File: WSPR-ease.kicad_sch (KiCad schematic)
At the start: 31 parts, among them J1 GNSS Ant, J2 Tx Ant, J3 USB_C_16P_Stacked, Q1 MMBF170, U1 ESP32-S3-WROOM-1-N8R8, U2 NCP1117-3.3_SOT223, U3 ATGM336H-5N31

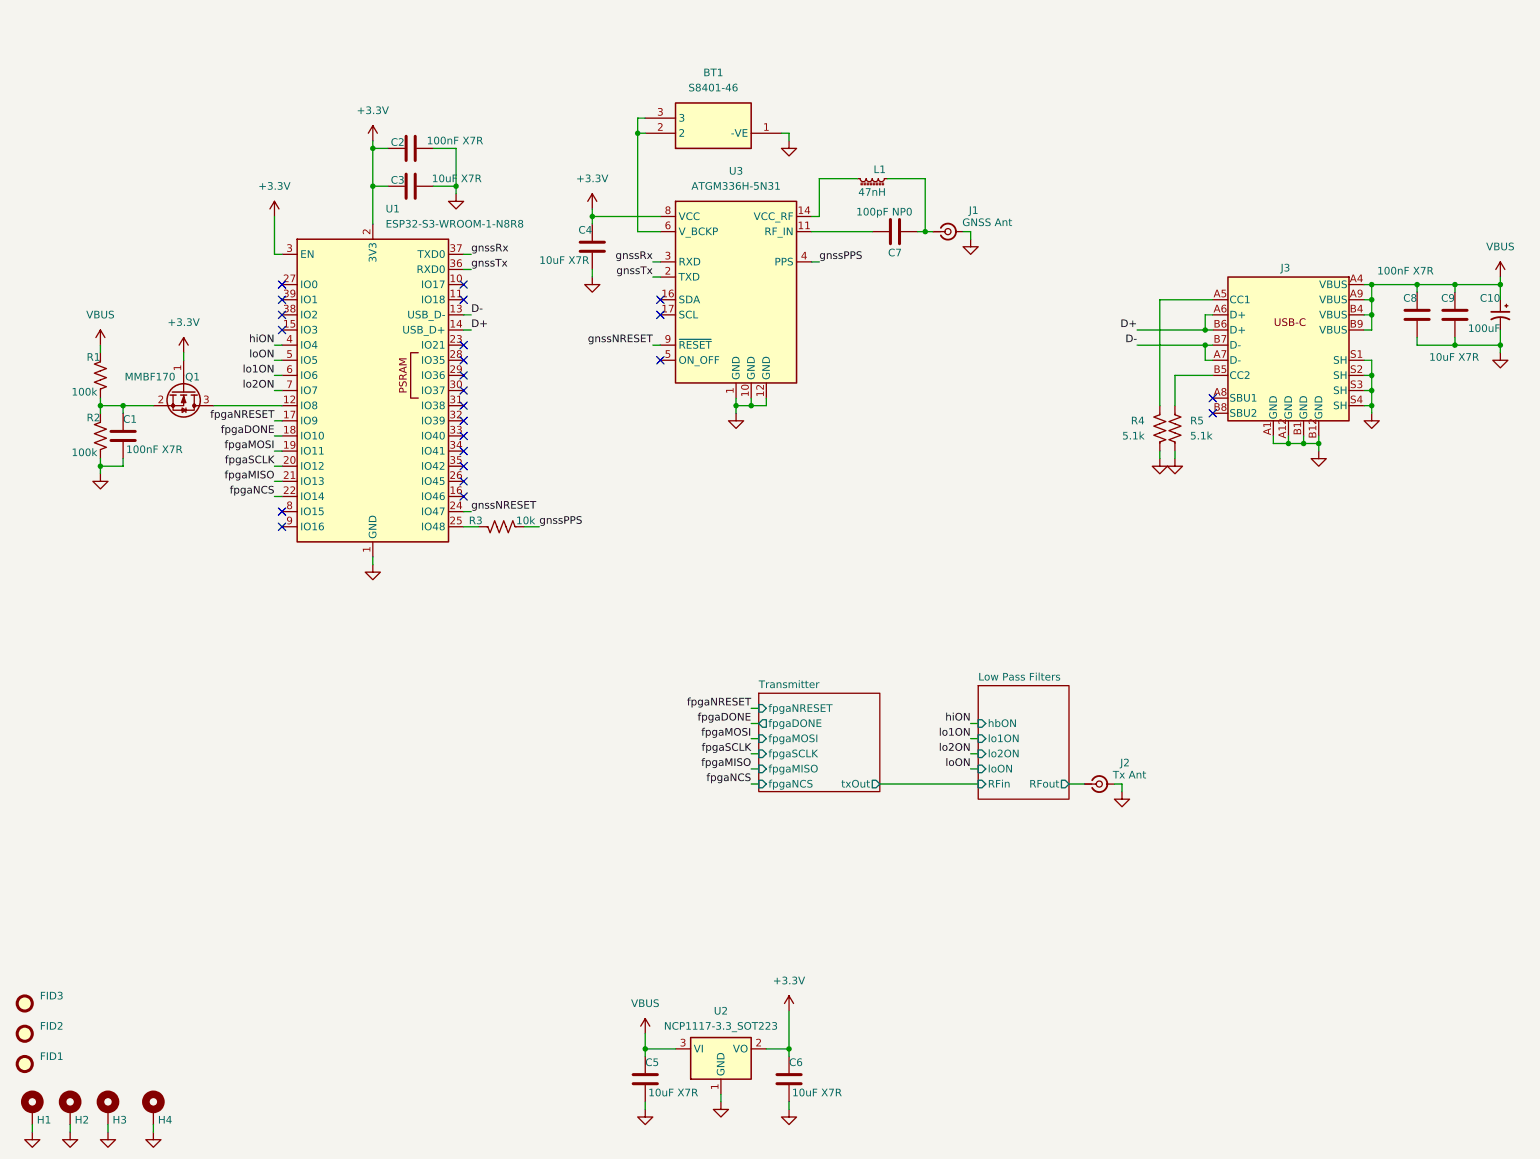
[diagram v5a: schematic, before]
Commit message: Cleanup. Better USB diff pair with 0ohm and TVS as recommended. Return to rectangular outline and even smaller. Mounting holes are consistently placed relative to board corners.
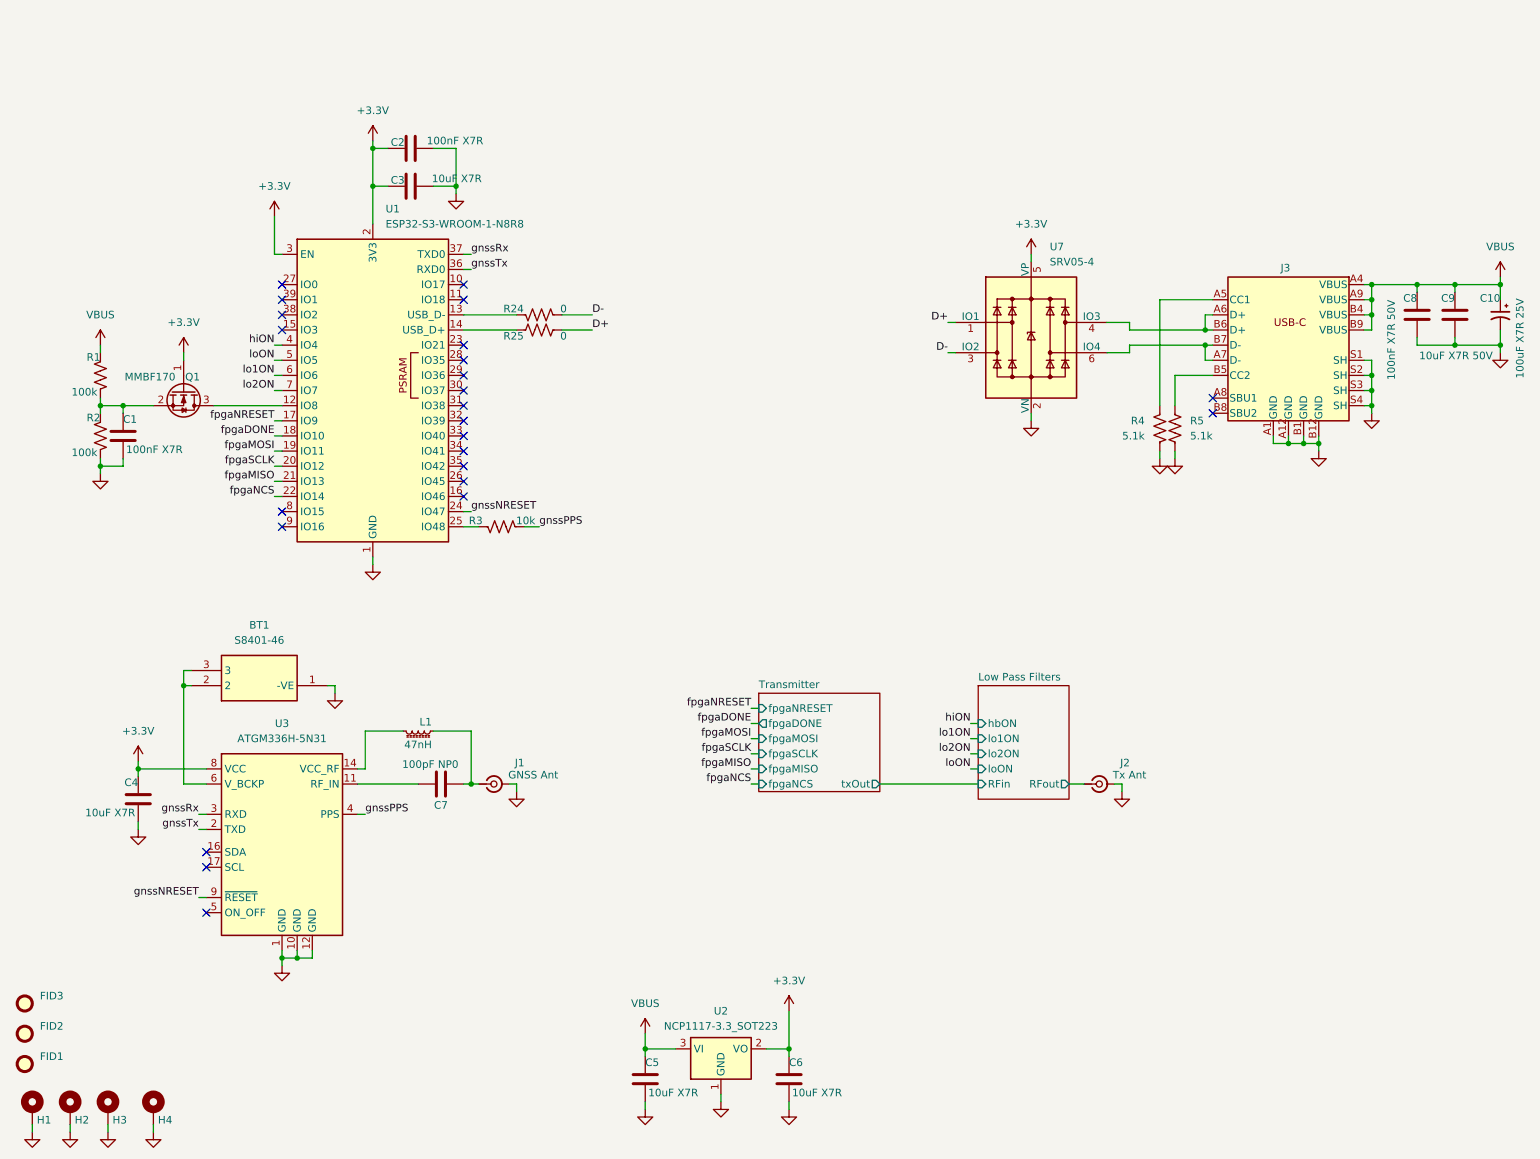
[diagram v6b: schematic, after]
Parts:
- added R24, R25: 0, Resistor_SMD:R_0402_1005Metric, symbol Device:R_US
- added U7: SRV05-4, Package_TO_SOT_SMD:SOT-23-6, symbol Power_Protection:SRV05-4
- C10: value 100uF -> 100uF X7R 25V
- C8: value 100nF X7R -> 100nF X7R 50V
- C9: value 10uF X7R -> 10uF X7R 50V
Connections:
- net +3.3V: now also U7.5 (VP)
- net D+: now also R25.2, U7.1 (IO1); no longer J3.A6 (D+), J3.B6 (D+), U1.14 (USB_D+)
- net D-: now also R24.2, U7.3 (IO2); no longer J3.A7 (D-), J3.B7 (D-), U1.13 (USB_D-)
- net GND: now also U7.2 (VN)
- new net: R24.1, U1.13 (USB_D-)
- new net: J3.A6 (D+), J3.B6 (D+), U7.4 (IO3)
- new net: J3.A7 (D-), J3.B7 (D-), U7.6 (IO4)
- new net: R25.1, U1.14 (USB_D+)
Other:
- moved on the sheet: BT1, C4, C7, J1, L1, U3

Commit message: Fix up 3d in footprints in lib so they stay put when I update PCB from schematic. Fix text labels for same issue.
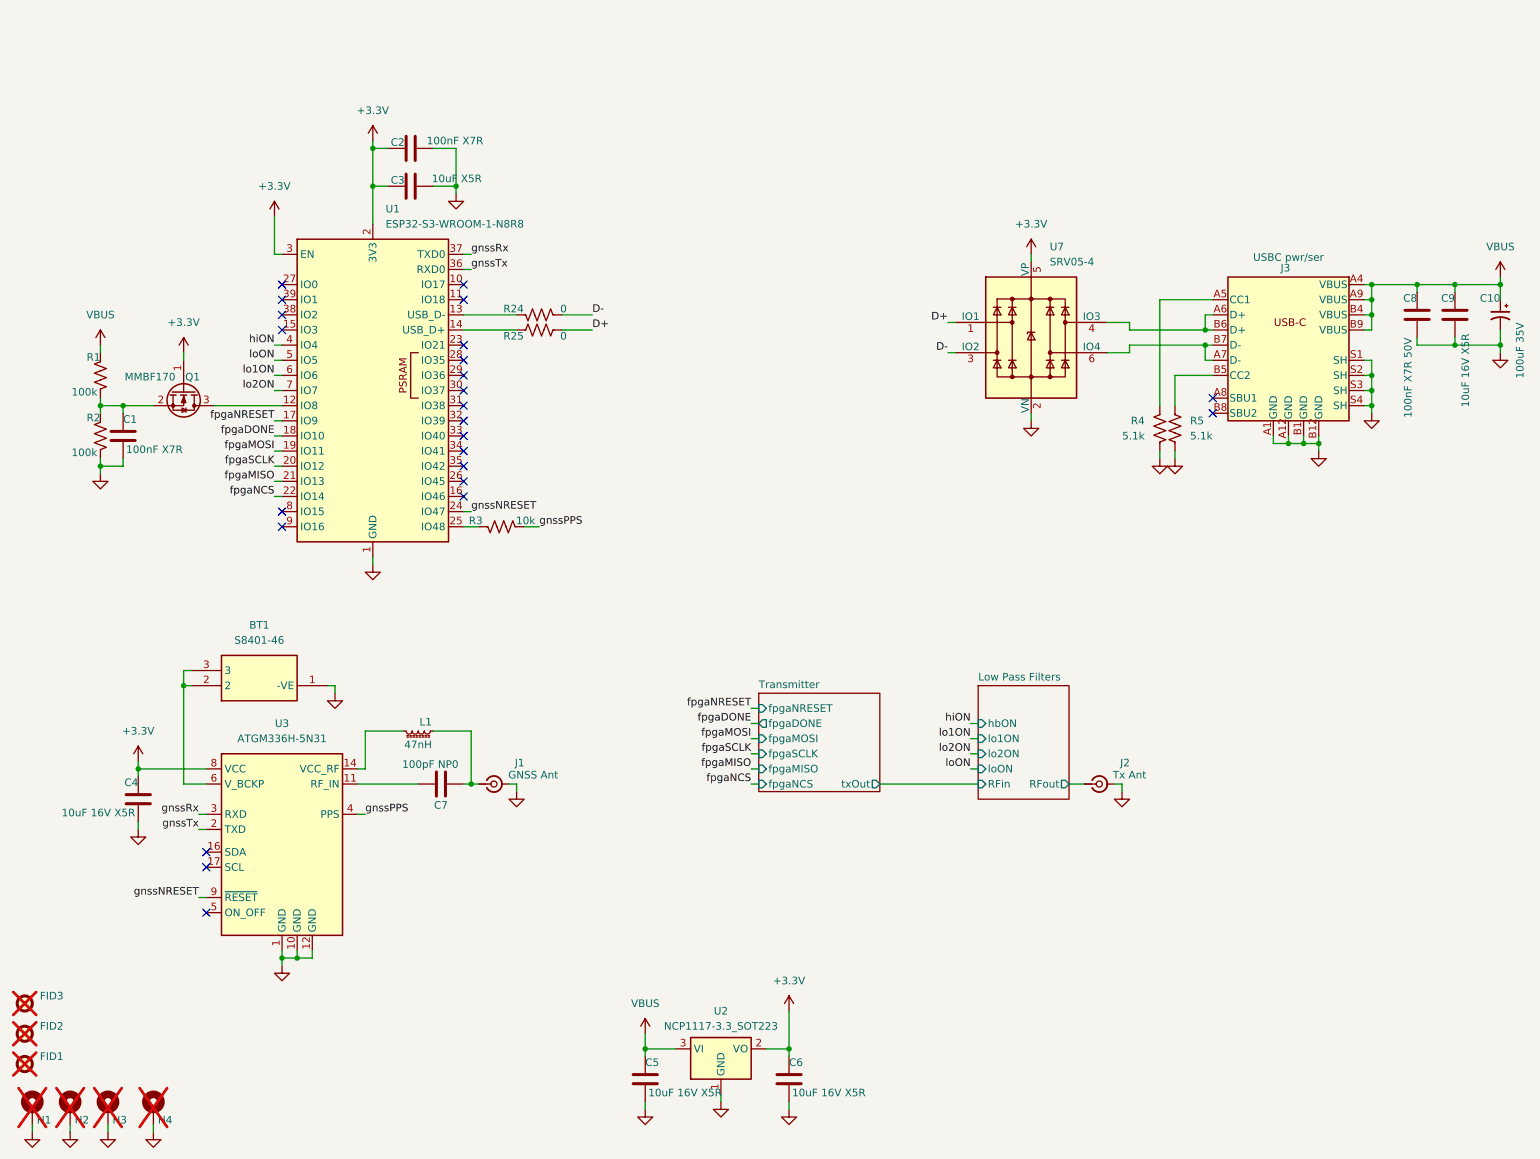
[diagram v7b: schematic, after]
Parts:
- C10: value 100uF X7R 25V -> 100uF 35V
- C3: value 10uF X7R -> 10uF X5R
- C4, C5, C6: value 10uF X7R -> 10uF 16V X5R; LCSC C32635 -> C1713
- C9: value 10uF X7R 50V -> 10uF 16V X5R; LCSC C32635 -> C1713
- FID1, FID2, FID3, H1, H2, H3, H4: now not fitted
- J3: label (none) -> USBC pwr/ser
- U7: LCSC (none) -> C2836319
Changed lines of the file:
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@@
 		(in_bom no)
 		(on_board yes)
-		(dnp no)
+		(dnp yes)
 		(property "Reference" "H3"
 			(at 29.972 198.628 0)
@@
 		)
 		(property "Value" "100nF X7R 50V"
-			(at 244.602 74.422 90)
+			(at 247.396 80.772 90)
 			(effects
 				(font
@@
 			)
 		)
+		(property "label" "USBC pwr/ser"
+			(at 227.33 53.848 0)
+			(effects
+				(font
+					(size 1.27 1.27)
+				)
+			)
+		)
 		(pin "A4"
 		)
@@
 			)
 		)
+		(property "LCSC" "C2836319"
+			(at 184.15 67.31 0)
+			(effects
+				(font
+					(size 1.27 1.27)
+				)
+				(hide yes)
+			)
+		)
 		(pin "2"
 		)
@@
 		(in_bom no)
 		(on_board yes)
-		(dnp no)
+		(dnp yes)
 		(property "Reference" "H1"
 			(at 17.272 198.628 0)
@@
 		(in_bom no)
 		(on_board yes)
-		(dnp no)
+		(dnp yes)
 		(fields_autoplaced yes)
 		(property "Reference" "FID1"
@@
 			)
 		)
-		(property "Value" "10uF X7R"
+		(property "Value" "10uF 16V X5R"
 			(at 144.018 194.056 0)
 			(effects
@@
 			)
 		)
-		(property "LCSC" "C32635"
+		(property "LCSC" "C1713"
 			(at 143.51 191.77 0)
 			(effects
@@
 		(in_bom no)
 		(on_board yes)
-		(dnp no)
+		(dnp yes)
 		(property "Reference" "H4"
 			(at 37.592 198.628 0)
@@
 		(in_bom no)
 		(on_board yes)
-		(dnp no)
+		(dnp yes)
 		(fields_autoplaced yes)
 		(property "Reference" "FID3"
@@
 			)
 		)
-		(property "Value" "10uF X7R 50V"
-			(at 261.62 70.358 0)
+		(property "Value" "10uF 16V X5R"
+			(at 257.048 78.994 90)
 			(effects
 				(font
@@
 			)
 		)
-		(property "LCSC" "C32635"
+		(property "LCSC" "C1713"
 			(at 255.27 63.5 0)
 			(effects
@@
 			)
 		)
-		(property "Value" "10uF X7R"
+		(property "Value" "10uF 16V X5R"
 			(at 119.888 194.056 0)
 			(effects
@@
 			)
 		)
-		(property "LCSC" "C32635"
+		(property "LCSC" "C1713"
 			(at 119.38 191.77 0)
 			(effects
@@
 			)
 		)
-		(property "Value" "10uF X7R"
+		(property "Value" "10uF X5R"
 			(at 91.948 40.64 90)
 			(effects
@@
 		(in_bom no)
 		(on_board yes)
-		(dnp no)
+		(dnp yes)
 		(fields_autoplaced yes)
 		(property "Reference" "FID2"
@@
 			)
 		)
-		(property "Value" "10uF X7R"
+		(property "Value" "10uF 16V X5R"
 			(at 33.782 147.066 0)
 			(effects
@@
 			)
 		)
-		(property "LCSC" "C32635"
+		(property "LCSC" "C1713"
 			(at 34.29 144.78 0)
 			(effects
@@
 		(in_bom no)
 		(on_board yes)
-		(dnp no)
+		(dnp yes)
 		(property "Reference" "H2"
 			(at 23.622 198.628 0)
@@
 			)
 		)
-		(property "Value" "100uF X7R 25V"
+		(property "Value" "100uF 35V"
 			(at 266.192 74.168 90)
 			(effects

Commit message: Fixes to pass ERC. Nothing serious really.
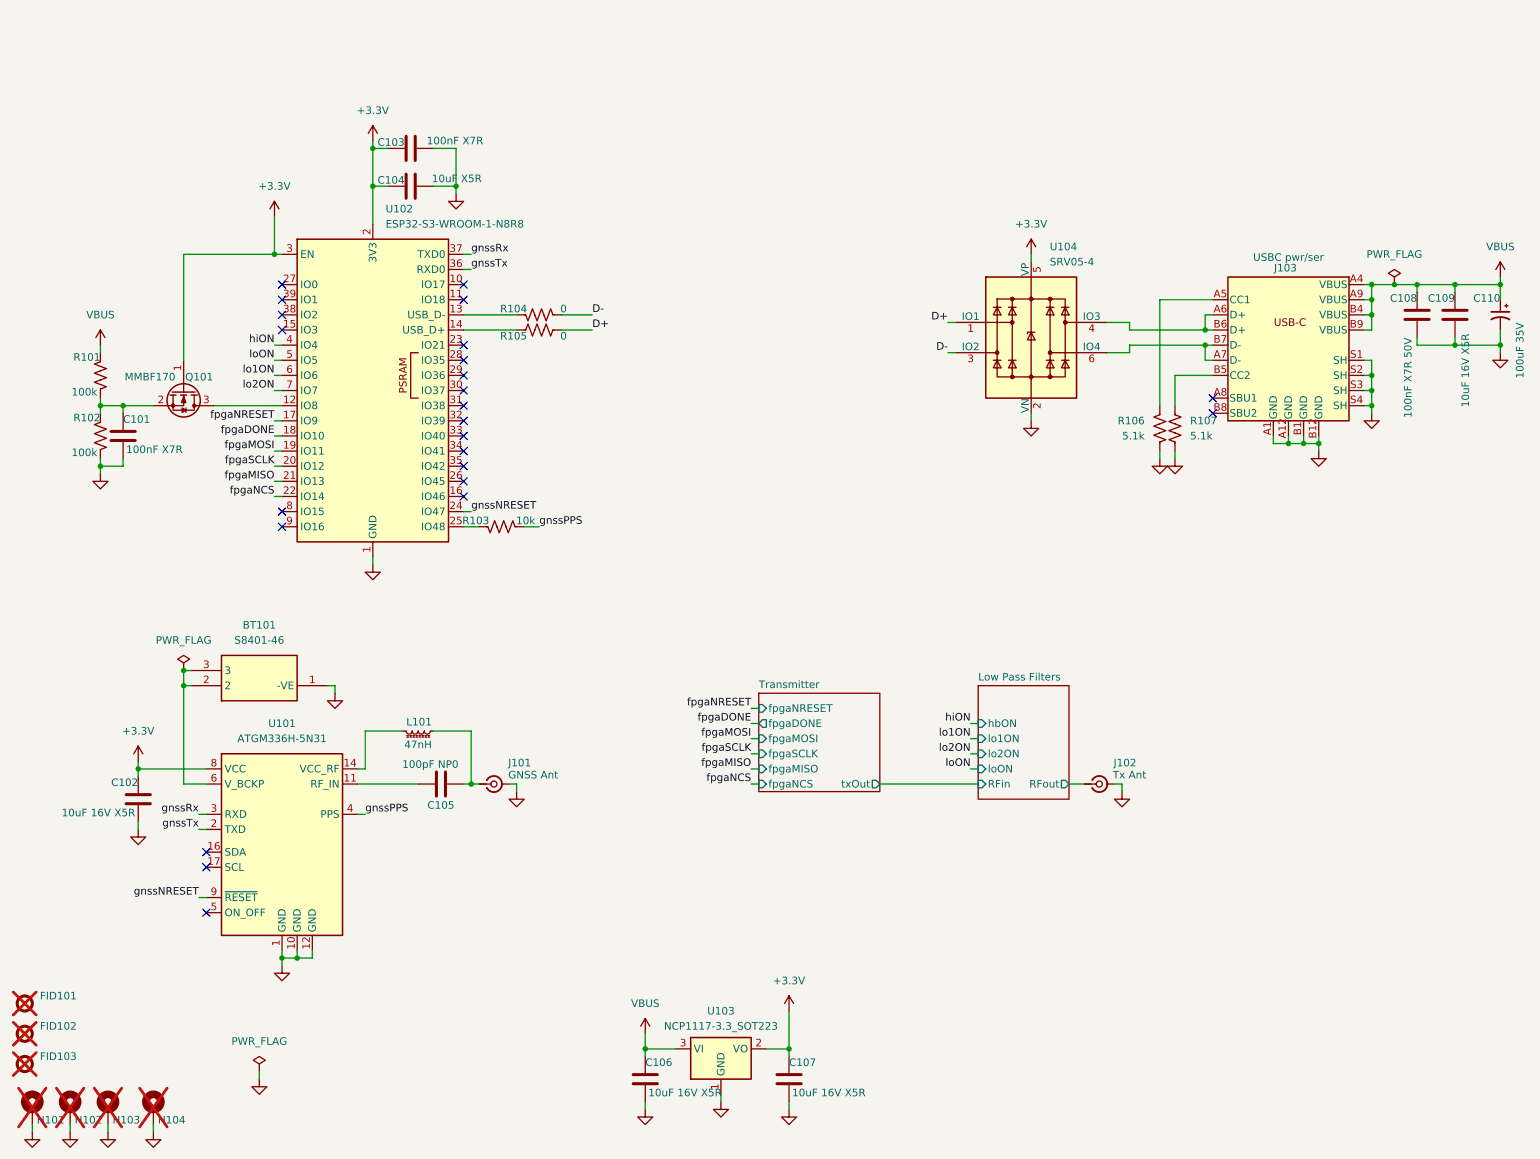
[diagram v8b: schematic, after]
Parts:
- BT101: renamed from BT1; footprint S8401-46 -> Library:S8401-46
- J103: renamed from J3; footprint Library:HRO-TYPE-C-31-M-12 -> Connector_USB:USB_C_Receptacle_HRO_TYPE-C-31-M-12
- renumbered C1 to C101, C4 to C102, C2 to C103, C3 to C104, C7 to C105, C5 to C106, C6 to C107, C8 to C108, C9 to C109, C10 to C110, FID3 to FID101, FID2 to FID102, FID1 to FID103, H1 to H101, H2 to H102, H3 to H103, H4 to H104, J1 to J101, J2 to J102, L1 to L101, Q1 to Q101, R1 to R101, R2 to R102, R3 to R103, R24 to R104, R25 to R105, R4 to R106, R5 to R107, U3 to U101, U1 to U102, U2 to U103, U7 to U104
